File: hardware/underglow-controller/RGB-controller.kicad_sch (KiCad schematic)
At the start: 141 parts, among them J2 U.FL-R-SMT-1(10), J3 DM3AT-SF-PEJM5, J4 DTM1312PA12PBR008, J5 Conn_01x10, J6 CONSOLE, J7 U.FL-R-SMT-1(10), J8 JTAG, Q2 Q_Dual_NMOS_S1G1S2G2D2D2D1D1, Q3 Q_Dual_NMOS_S1G1S2G2D2D2D1D1, Q4 Q_Dual_NMOS_S1G1S2G2D2D2D1D1, SW2 SW_Push, SW3 SW_Push, SW4 SW_Push, U10 DRV8844PWP, U11 RP2040, U2 ESP-PSRAM32, U3 SN65HVD230, U4 ESP32-S3R2, U5 W25Q128JVS, U6 WS2815B, U7 W25Q128JVS, U8 ADP2303ARDZ-3.3, U9 COM-13909, Y2 40MHZ, Y3 32.7k, Y4 40MHZ

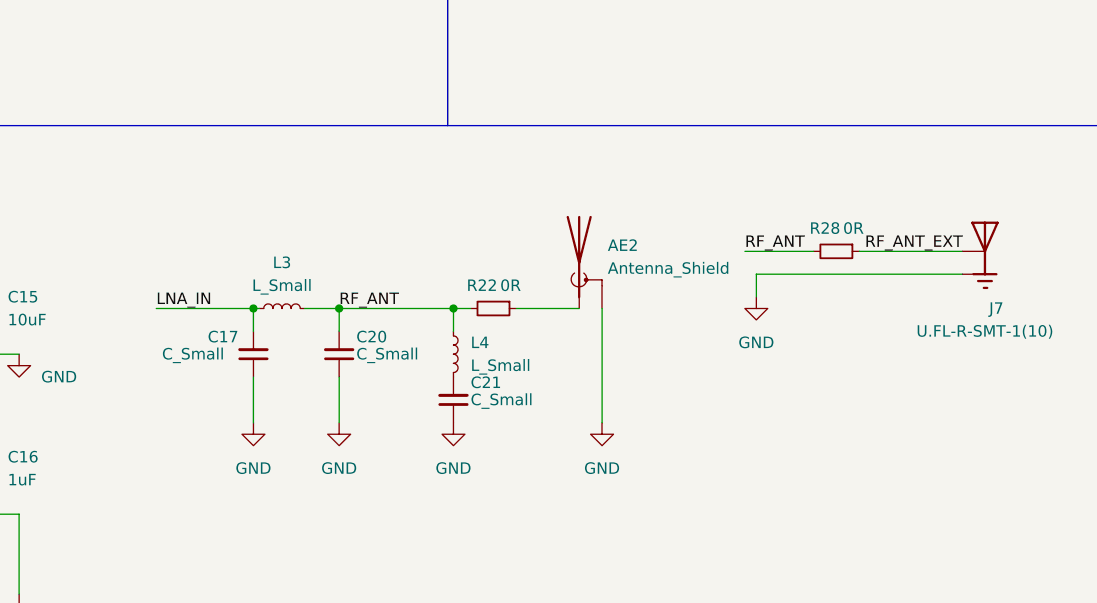
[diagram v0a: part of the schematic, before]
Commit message: Calculate initial values for antenna resistor matching network
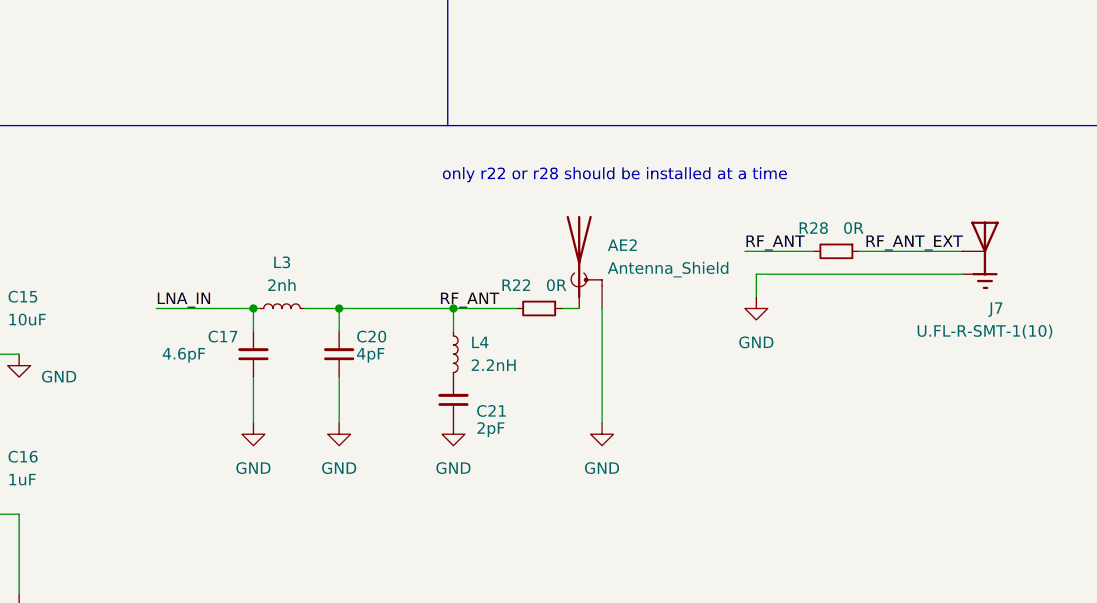
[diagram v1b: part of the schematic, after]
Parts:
- C17: value C_Small -> 4.6pF
- C20: value C_Small -> 4pF
- C21: value C_Small -> 2pF
- L3: value L_Small -> 2nh
- L4: value L_Small -> 2.2nH
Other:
- note added: "only r22 or r28 should be installed at a time"
- moved on the sheet: R22
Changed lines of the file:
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@@
     (stroke (width 0) (type default) (color 0 0 0 0))
   )
-  (wire (pts (xy 354.33 129.54) (xy 361.315 129.54))
+  (wire (pts (xy 359.41 129.54) (xy 361.315 129.54))
     (stroke (width 0) (type default) (color 0 0 0 0))
   )
@@
     (stroke (width 0) (type default) (color 0 0 0 0))
   )
-  (wire (pts (xy 347.345 129.54) (xy 349.25 129.54))
+  (wire (pts (xy 347.345 129.54) (xy 354.33 129.54))
     (stroke (width 0) (type default) (color 0 0 0 0))
   )
@@
     (effects (font (size 3 3)) (justify right bottom))
   )
+  (text "only r22 or r28 should be installed at a time" (at 346.075 115.57 0)
+    (effects (font (size 1.27 1.27)) (justify left bottom))
+  )
   (text "Main outer connector" (at 43.18 70.485 0)
     (effects (font (size 1 1)) (justify left bottom))
@@
     (effects (font (size 1.27 1.27)) (justify left bottom))
   )
-  (label "RF_ANT" (at 334.645 129.54 0)
-    (effects (font (size 1.27 1.27)) (justify left bottom))
+  (label "RF_ANT" (at 352.425 129.54 180)
+    (effects (font (size 1.27 1.27)) (justify right bottom))
   )
   (label "GPIO12" (at 203.835 189.23 180)
@@
     (effects (font (size 1.27 1.27)) (justify right bottom))
   )
-  (symbol (lib_id "Device:R_Small") (at 351.79 129.54 270) (unit 1)
+  (symbol (lib_id "Device:R_Small") (at 356.87 129.54 270) (unit 1)
     (in_bom yes) (on_board yes)
-    (property "Reference" "R22" (id 0) (at 350.52 127 90))
-    (property "Value" "0R" (id 1) (at 353.695 127 90))
-    (property "Footprint" "Resistor_SMD:R_0402_1005Metric" (id 2) (at 351.79 129.54 0)
+    (property "Reference" "R22" (id 0) (at 354.33 127 90))
+    (property "Value" "0R" (id 1) (at 358.775 127 90))
+    (property "Footprint" "Resistor_SMD:R_0402_1005Metric" (id 2) (at 356.87 129.54 0)
       (effects (font (size 1.27 1.27)) hide)
     )
-    (property "Datasheet" "~" (id 3) (at 351.79 129.54 0)
+    (property "Datasheet" "~" (id 3) (at 356.87 129.54 0)
       (effects (font (size 1.27 1.27)) hide)
     )
@@
       (effects (font (size 1.27 1.27)) (justify left))
     )
-    (property "Value" "L_Small" (id 1) (at 349.25 135.8899 0)
+    (property "Value" "2.2nH" (id 1) (at 349.25 135.8899 0)
       (effects (font (size 1.27 1.27)) (justify left))
     )
@@
   (symbol (lib_id "Device:R_Small") (at 389.89 123.19 270) (unit 1)
     (in_bom yes) (on_board yes)
-    (property "Reference" "R28" (id 0) (at 388.62 120.65 90))
+    (property "Reference" "R28" (id 0) (at 387.35 120.65 90))
     (property "Value" "0R" (id 1) (at 391.795 120.65 90))
     (property "Footprint" "Resistor_SMD:R_0402_1005Metric" (id 2) (at 389.89 123.19 0)
@@
       (effects (font (size 1.27 1.27)) (justify right))
     )
-    (property "Value" "C_Small" (id 1) (at 314.96 134.6135 0)
+    (property "Value" "4.6pF" (id 1) (at 314.96 134.6135 0)
       (effects (font (size 1.27 1.27)) (justify right))
     )
@@
       (effects (font (size 1.27 1.27)) (justify right))
     )
-    (property "Value" "C_Small" (id 1) (at 336.55 134.6135 0)
+    (property "Value" "4pF" (id 1) (at 336.55 134.6135 0)
       (effects (font (size 1.27 1.27)) (justify right))
     )
@@
   (symbol (lib_id "Device:C_Small") (at 347.345 139.7 180) (unit 1)
     (in_bom yes) (on_board yes)
-    (property "Reference" "C21" (id 0) (at 349.25 137.7885 0)
+    (property "Reference" "C21" (id 0) (at 349.885 140.97 0)
       (effects (font (size 1.27 1.27)) (justify right))
     )
-    (property "Value" "C_Small" (id 1) (at 349.25 139.6935 0)
+    (property "Value" "2pF" (id 1) (at 349.885 142.875 0)
       (effects (font (size 1.27 1.27)) (justify right))
     )
@@
     (in_bom yes) (on_board yes) (fields_autoplaced)
     (property "Reference" "L3" (id 0) (at 328.295 124.46 90))
-    (property "Value" "L_Small" (id 1) (at 328.295 127 90))
+    (property "Value" "2nh" (id 1) (at 328.295 127 90))
     (property "Footprint" "Inductor_SMD:L_0402_1005Metric" (id 2) (at 328.295 129.54 0)
       (effects (font (size 1.27 1.27)) hide)
@@
     )
     (path "/b9ab7816-1c29-4976-8db3-b109e2a5a52a"
-      (reference "C17") (unit 1) (value "C_Small") (footprint "Capacitor_SMD:C_0402_1005Metric")
+      (reference "C17") (unit 1) (value "4.6pF") (footprint "Capacitor_SMD:C_0402_1005Metric")
     )
     (path "/7e0b0922-d79e-425d-9f0a-c8f846c46c70"
@@
     )
     (path "/bd83965e-06bc-43f3-8da4-0d2f6c82feed"
-      (reference "C20") (unit 1) (value "C_Small") (footprint "Capacitor_SMD:C_0402_1005Metric")
+      (reference "C20") (unit 1) (value "4pF") (footprint "Capacitor_SMD:C_0402_1005Metric")
     )
     (path "/c66ee995-4b17-4397-a6fe-1e1196abf8d6"
-      (reference "C21") (unit 1) (value "C_Small") (footprint "Capacitor_SMD:C_0402_1005Metric")
+      (reference "C21") (unit 1) (value "2pF") (footprint "Capacitor_SMD:C_0402_1005Metric")
     )
     (path "/de4cb496-992c-4012-9925-79f1c3a28906"
@@
     )
     (path "/d87ba769-25c6-47a5-9081-6d1f0efd4a0d"
-      (reference "L3") (unit 1) (value "L_Small") (footprint "Inductor_SMD:L_0402_1005Metric")
+      (reference "L3") (unit 1) (value "2nh") (footprint "Inductor_SMD:L_0402_1005Metric")
     )
     (path "/5b1fe326-922f-49d7-b9e2-a3fa79272f74"
-      (reference "L4") (unit 1) (value "L_Small") (footprint "Inductor_SMD:L_0402_1005Metric")
+      (reference "L4") (unit 1) (value "2.2nH") (footprint "Inductor_SMD:L_0402_1005Metric")
     )
     (path "/c5d66d2f-e116-412b-ace5-f14ec6de13ea"

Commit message: Calculate clock values
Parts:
- C18, C22: value C_Small -> 16pF
- C19, C23: value C_Small -> 10pF
- C24, C26: value C_Small -> 20pF
- Y3: MPN (none) -> ABS07-32.768KHZ-7-T
- Y4: MPN ECS-400-10-37B2-CKY-TR -> ABM8-12.000MHZ-12-B1U-T
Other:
- note added: "CX1 = CX2 = 2(10pF - 2pF) = 16pF"
- note added: "CX1 = CX2 = 2(12pF - 2pF) = 20pF"
- note added: "CX1 = CX2 = 2(7pF - 2pF) = 10pF"
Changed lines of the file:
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@@
     (effects (font (size 1.27 1.27)) (justify left bottom))
   )
+  (text "CX1 = CX2 = 2(7pF - 2pF) = 10pF" (at 285.75 213.36 0)
+    (effects (font (size 1.27 1.27)) (justify left bottom))
+  )
   (text "CAN" (at 107.315 18.415 180)
     (effects (font (size 3 3)) (justify right bottom))
@@
     (effects (font (size 3 3)) (justify right bottom))
   )
+  (text "CX1 = CX2 = 2(12pF - 2pF) = 20pF" (at 388.62 257.175 0)
+    (effects (font (size 1.27 1.27)) (justify left bottom))
+  )
   (text "MOTOR DRIVER" (at 370.84 337.185 0)
     (effects (font (size 3 3)) (justify left bottom))
@@
     (effects (font (size 2.54 2.54)) (justify left bottom))
   )
+  (text "CX1 = CX2 = 2(10pF - 2pF) = 16pF" (at 291.465 190.5 0)
+    (effects (font (size 1.27 1.27)) (justify left bottom))
+  )
   (label "GPIO12" (at 203.835 189.23 180)
     (effects (font (size 1.27 1.27)) (justify right bottom))
@@
       (effects (font (size 1.27 1.27)) (justify left))
     )
-    (property "Value" "C_Small" (id 1) (at 297.815 202.5712 0)
+    (property "Value" "10pF" (id 1) (at 297.815 202.5712 0)
       (effects (font (size 1.27 1.27)) (justify left))
     )
@@
       (effects (font (size 1.27 1.27)) (justify left))
     )
-    (property "Value" "C_Small" (id 1) (at 425.45 247.6562 0)
+    (property "Value" "20pF" (id 1) (at 425.45 247.6562 0)
       (effects (font (size 1.27 1.27)) (justify left))
     )
@@
   (symbol (lib_id "Device:Crystal_GND24_Small") (at 408.94 243.205 0) (unit 1)
     (in_bom yes) (on_board yes)
-    (property "Reference" "Y4" (id 0) (at 405.13 235.585 0))
+    (property "Reference" "Y4" (id 0) (at 403.225 236.855 0))
     (property "Value" "40MHZ" (id 1) (at 415.29 240.03 0))
     (property "Footprint" "Crystal:Crystal_SMD_3225-4Pin_3.2x2.5mm" (id 2) (at 408.94 243.205 0)
@@
       (effects (font (size 1.27 1.27)) hide)
     )
-    (property "MPN" "ECS-400-10-37B2-CKY-TR" (id 4) (at 408.94 243.205 0)
+    (property "MPN" "ABM8-12.000MHZ-12-B1U-T" (id 4) (at 408.94 243.205 0)
       (effects (font (size 1.27 1.27)) hide)
     )
@@
       (effects (font (size 1.27 1.27)) (justify left))
     )
-    (property "Value" "C_Small" (id 1) (at 255.905 186.0612 0)
+    (property "Value" "16pF" (id 1) (at 255.905 186.0612 0)
       (effects (font (size 1.27 1.27)) (justify left))
     )
@@
       (effects (font (size 1.27 1.27)) hide)
     )
+    (property "MPN" "ABS07-32.768KHZ-7-T" (id 4) (at 278.13 198.12 0)
+      (effects (font (size 1.27 1.27)) hide)
+    )
     (pin "1")
     (pin "2")
@@
       (effects (font (size 1.27 1.27)) (justify left))
     )
-    (property "Value" "C_Small" (id 1) (at 391.795 247.6562 0)
+    (property "Value" "20pF" (id 1) (at 391.795 247.6562 0)
       (effects (font (size 1.27 1.27)) (justify left))
     )
@@
       (effects (font (size 1.27 1.27)) (justify left))
     )
-    (property "Value" "C_Small" (id 1) (at 256.54 202.5712 0)
+    (property "Value" "10pF" (id 1) (at 256.54 202.5712 0)
       (effects (font (size 1.27 1.27)) (justify left))
     )
@@
       (effects (font (size 1.27 1.27)) (justify left))
     )
-    (property "Value" "C_Small" (id 1) (at 297.18 186.0612 0)
+    (property "Value" "16pF" (id 1) (at 297.18 186.0612 0)
       (effects (font (size 1.27 1.27)) (justify left))
     )
@@
     )
     (path "/7e0b0922-d79e-425d-9f0a-c8f846c46c70"
-      (reference "C18") (unit 1) (value "C_Small") (footprint "Capacitor_SMD:C_0402_1005Metric")
+      (reference "C18") (unit 1) (value "16pF") (footprint "Capacitor_SMD:C_0402_1005Metric")
     )
     (path "/dc9a55cb-741e-45c7-93b1-8310aff679c5"
-      (reference "C19") (unit 1) (value "C_Small") (footprint "Capacitor_SMD:C_0402_1005Metric")
+      (reference "C19") (unit 1) (value "10pF") (footprint "Capacitor_SMD:C_0402_1005Metric")
     )
     (path "/bd83965e-06bc-43f3-8da4-0d2f6c82feed"
@@
     )
     (path "/de4cb496-992c-4012-9925-79f1c3a28906"
-      (reference "C22") (unit 1) (value "C_Small") (footprint "Capacitor_SMD:C_0402_1005Metric")
+      (reference "C22") (unit 1) (value "16pF") (footprint "Capacitor_SMD:C_0402_1005Metric")
     )
     (path "/275d5c12-db5c-4d63-9a5a-01a3021371a0"
-      (reference "C23") (unit 1) (value "C_Small") (footprint "Capacitor_SMD:C_0402_1005Metric")
+      (reference "C23") (unit 1) (value "10pF") (footprint "Capacitor_SMD:C_0402_1005Metric")
     )
     (path "/d6a3d135-1352-4ee6-ab91-cd98f3d9c838"
-      (reference "C24") (unit 1) (value "C_Small") (footprint "Capacitor_SMD:C_0402_1005Metric")
+      (reference "C24") (unit 1) (value "20pF") (footprint "Capacitor_SMD:C_0402_1005Metric")
     )
     (path "/fc0df37a-04c0-4230-99ea-4c859d61ef50"
@@
     )
     (path "/3335745b-dfbc-4b80-8f94-44b1728137fe"
-      (reference "C26") (unit 1) (value "C_Small") (footprint "Capacitor_SMD:C_0402_1005Metric")
+      (reference "C26") (unit 1) (value "20pF") (footprint "Capacitor_SMD:C_0402_1005Metric")
     )
     (path "/a4458d84-6acc-4674-a192-795779d014ed"

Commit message: start filling out BOM
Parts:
- removed C3: 0.1uF, Capacitor_SMD:C_0402_1005Metric, symbol Device:C_Small
- removed R5: 100k, Resistor_SMD:R_0402_1005Metric, symbol Device:R_Small
- removed U2: ESP-PSRAM32, Package_SO:SOIC-8_3.9x4.9mm_P1.27mm, symbol Memory_RAM:ESP-PSRAM32
- AE2: value Antenna_Shield -> PCB_ANT
- AE3: value Antenna_Shield -> PCB_ANT_RFM69
- C12, C15: MPN (none) -> 04026D106MAT2A
- C17: MPN (none) -> 04023J4R6ABSTR
- C18, C22: MPN (none) -> 04025A160JAT2A
- C20: MPN (none) -> 04025J4R0ABSTR
- C21: MPN (none) -> 04023J2R0ABSTR
- L3: value 2nh -> 2nH
- Q2, Q3, Q4: value Q_Dual_NMOS_S1G1S2G2D2D2D1D1 -> STS8DNF3LL
- R41, R42: value 27R4 -> 27r4
- U11: MPN (none) -> RP2040
- U5, U7: MPN (none) -> W25Q128JVS
- U6: MPN (none) -> WS2815B
- U8: MPN (none) -> ADP2303ARDZ-3.3

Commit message: Fill out BOM for mouser
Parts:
- removed C2: 1uF, Capacitor_SMD:C_0402_1005Metric, symbol Device:C_Small
- removed R2: 442k, Resistor_SMD:R_0402_1005Metric, symbol Device:R_Small
- C10, C14, C29, C31, C35, C4, C40, C48, C49, C50, C51, C52, C7, C8, C9: MPN (none) -> 04023C104KAT4A
- C11, C13, C16, C28, C33, C37, C38: MPN (none) -> 04023D105KAT2A
- C19, C23: MPN (none) -> C0402C100K5RACAUTO
- C24, C26: MPN (none) -> 06035A200JAT2A
- C25, C44, C45, C5: MPN (none) -> 0805YC106KAT2A
- C32, C43, C6: MPN (none) -> 08055C104M4T4A
- C39, C41: MPN (none) -> 08056D226MAT2A
- C42: MPN (none) -> 0805ZC474MAT2A
- C46: MPN (none) -> C0805C103J3GACAUTO
- C47: MPN (none) -> EDH106M050A9DAA
- D2, D4: MPN (none) -> 150060VS75000
- D3: MPN (none) -> 150060SS75003
- D5: footprint Diode_SMD:D_SOD-123 -> Diode_SMD:D_SOD-123F; MPN PMEG3015EH,115 -> RB070MM-30TR
- L3: MPN (none) -> MHQ0402PSA22NHT000
- L4: MPN (none) -> LCCI0402S2N2GTAR
- R10, R11, R12, R13, R16, R17, R22, R28, R32, R33, R7, R8, R9: MPN (none) -> AC0402JR-070RL
- R14, R36: MPN (none) -> RT0402FRE071KL
- R15, R37: MPN (none) -> AC0402FR-07100KL
- R23: value 100k -> 10k; MPN (none) -> RC0603FR-0710KL
- R24, R25, R26, R27, R31, R38, R4, R40, R43, R44, R45: MPN (none) -> RC0402FR-1010KL
- R30: MPN (none) -> AC0402JR-0736KL
- R34: MPN (none) -> CR0603-FX-3162ELF
- R35: MPN (none) -> CR0603-FX-1022ELF
- R39: footprint Resistor_SMD:R_0603_1608Metric -> Resistor_SMD:R_0402_1005Metric; MPN RMCF0603JT10K0 -> RC0603FR-0710KL
- R41, R42: MPN (none) -> CR0402-FX-27R4GLF
- R6: MPN (none) -> RC0402FR-13499RL
- SW2, SW3, SW4: MPN (none) -> RS032G05A3SMRT
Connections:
- net SPICLK_N: no longer names the net of U4.36 (SPICLK_N)
- net SPICLK_P: no longer names the net of U4.37 (SPICLK_P)
- no-connect marks 30 -> 32

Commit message: bom bom bom bom
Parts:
- C25: VOLTAGE 25V -> (none)
- C45, C5: MPN2 CC0402KRX5R8BB104 -> (none); Manufacturer Murata Electronics -> (none); Manufacturer2 Yageo -> (none)
- D5: DESCRIPTION DIODE SCHOTTKY 30V 1.5A SOD123F -> (none)
- J2, J7: DESCRIPTION U.FL Series 6 Ghz 50 Ohm Ultra-small SMT Coaxial Cable Rece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 -> (none); MANUFACTURER Hirose -> (none); MP U.FL-R-SMT-1_10_ -> (none); PRICE 0.71 USD -> (none); STANDARD Manufacturer Recommendation -> (none)
- J3: DESCRIPTION DM3 RA SMT microSD memory card push/push -> (none); LCSC (none) -> C114218; MF Hirose -> (none)
- L6: DESCRIPTION FIXED IND 6.8UH 2.2A 63 MOHM SMD -> (none)
- Q2, Q3, Q4: DESCRIPTION MOSFET N-CH 25V 8A 8SO -> (none); LCSC (none) -> C2971469
- R39: DESCRIPTION RES 10K OHM 5% 1/10W 0603 -> (none)
- U10: LCSC (none) -> C177807
- U11: LCSC (none) -> C2040
- U3: DESCRIPTION IC TRANSCEIVER HALF 1/1 8SOIC -> (none); LCSC (none) -> C12084
- U4: LCSC (none) -> C2913192
- U5, U7: LCSC (none) -> C113767
- U6: DESCRIPTION 12mA RGB SMD,5.4x5x1.65mm Light Emitting Diodes (LED) ROHS -> (none); LCSC (none) -> C965559; MPN WS2815B -> (none); automotive No -> (none); category IC -> (none); colour Blue, Green, Red -> (none); device class L1 Optoelectronics -> (none); device class L2 LEDs -> (none); device class L3 unset -> (none); height 1.7mm -> (none); lead free Unknown -> (none); led orientation Top View -> (none); library id e667c779cab89d9d -> (none); manufacturer worldsemi -> (none); max supply voltage 13.5V -> (none); min supply voltage 9.5V -> (none); output current 2.1mA -> (none); package SMD5050 -> (none); rohs Unknown -> (none); standoff height 0.13mm -> (none); temperature range high +85°C -> (none); temperature range low -25°C -> (none); wavelength 470/520/622.5nm -> (none)
- U8: LCSC (none) -> C659152
- U9: MANUFACTURER SparkFun Electronics -> (none)

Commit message: Submit for fab. tagme
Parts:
- C10, C14, C29, C31, C35, C4, C40, C48, C49, C50, C51, C52, C7, C8, C9: MPN 04023C104KAT4A -> C0805C104M3RAC7800
- C11, C13, C16, C28, C33, C37, C38: MPN 04023D105KAT2A -> CGA2B1X7T0G105M050BC
- C12, C15: MPN 04026D106MAT2A -> CL05X106MR5NUNC
- C17: MPN 04023J4R6ABSTR -> TMK042CG4R6BD-W
- C18, C22: MPN 04025A160JAT2A -> GCM1555C1H160JA16D
- C19, C23: MPN C0402C100K5RACAUTO -> C1005NP01H100D050BA
- C20: MPN 04025J4R0ABSTR -> UMK105UJ040CV-F
- C21: MPN 04023J2R0ABSTR -> UMK105CK020CVHF
- C24, C26: MPN 06035A200JAT2A -> CL05C200GB51PNC
- C25, C44, C45, C5: MPN 0805YC106KAT2A -> CL21A106KAFN3NE
- C32, C43, C6: MPN 08055C104M4T4A -> LMK212SD104KG-T
- C39, C41: MPN 08056D226MAT2A -> CL21A226MOQNNNE
- C42: MPN 0805ZC474MAT2A -> CGA4J3X7R1H474K125AB
- C46: MPN C0805C103J3GACAUTO -> C0805C103K1RAC7210
- C47: MPN EDH106M050A9DAA -> 106AXZ035M
- D2, D4: MPN 150060VS75000 -> QBLP601-2IR4
- D3: MPN 150060SS75003 -> QBLP601-R35
- D5: MPN RB070MM-30TR -> CUHS15S30,H3F
- L3: MPN MHQ0402PSA22NHT000 -> LQG15HN2N0C02D
- L4: MPN LCCI0402S2N2GTAR -> L-07C2N2SV6T
- L6: value 6.8uh -> 4.7uH; MPN SRN6028-6R8M -> SRN6028-4R7M
- R10, R11, R12, R13, R16, R17, R22, R28, R32, R33, R7, R8, R9: MPN AC0402JR-070RL -> (none)
- R14, R36: MPN RT0402FRE071KL -> RMCF0402FT1K00
- R15, R37: MPN AC0402FR-07100KL -> RNCF0402DTE100K
- R18, R19, R20: MPN (none) -> RMCF0402JT240R
- R21: MPN (none) -> RMCF2512ZT0R00
- R23: MPN RC0603FR-0710KL -> RNCP0603FTD10K0
- R24, R25, R26, R27, R31, R38, R4, R40, R43, R44, R45: MPN RC0402FR-1010KL -> RMCF0402JT10K0
- R3: MPN (none) -> RMCF0805JT120R
- R30: MPN AC0402JR-0736KL -> RC0402FR-0736KL
- R34: MPN CR0603-FX-3162ELF -> RC0603FR-0731K6L
- R35: MPN CR0603-FX-1022ELF -> RNCF0603DTE10K2
- R39: MPN RC0603FR-0710KL -> RMCF0402JT10K0
- R41, R42: MPN CR0402-FX-27R4GLF -> RMCF0402FT27R4
- R6: MPN RC0402FR-13499RL -> RMCF0402FT499R
- U11: MPN RP2040 -> SC0914(13)
- U9: MPN RFM69HCW -> COM-13909; MPN2 COM-13909 -> (none)
- Y4: value 40MHZ -> 12MHZ
